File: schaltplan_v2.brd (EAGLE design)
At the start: 101 x 80 mm, 42 parts, among them T1 2N3565, T2 2N3565, T3 2N3565, T4 2N3565, T5 2N3565, T6 2N3565, T7 2N3565, T8 2N3565

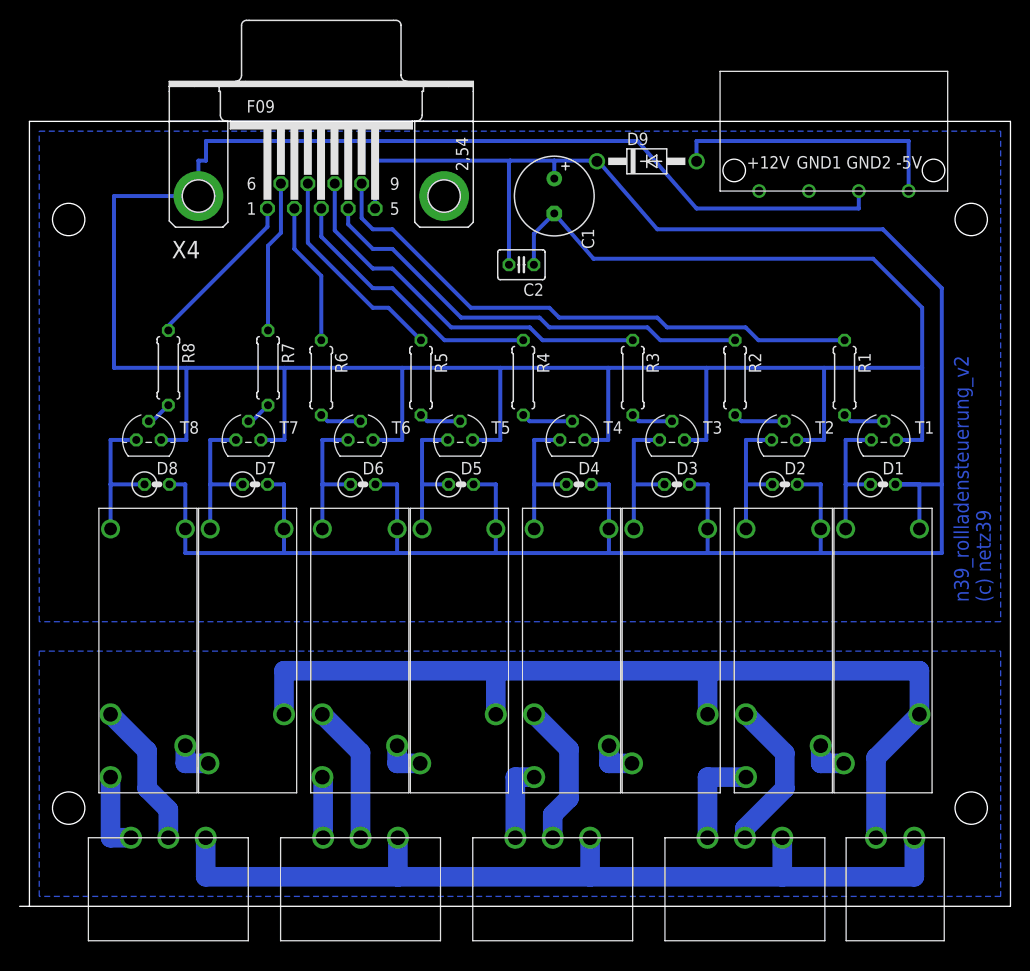
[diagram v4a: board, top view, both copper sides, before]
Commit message: fix ERC issues and schematic, reroute some signals
overall connection was lost due to some signal renamings, some parts
were not connected at all. additionally added restrict area around drill
holes
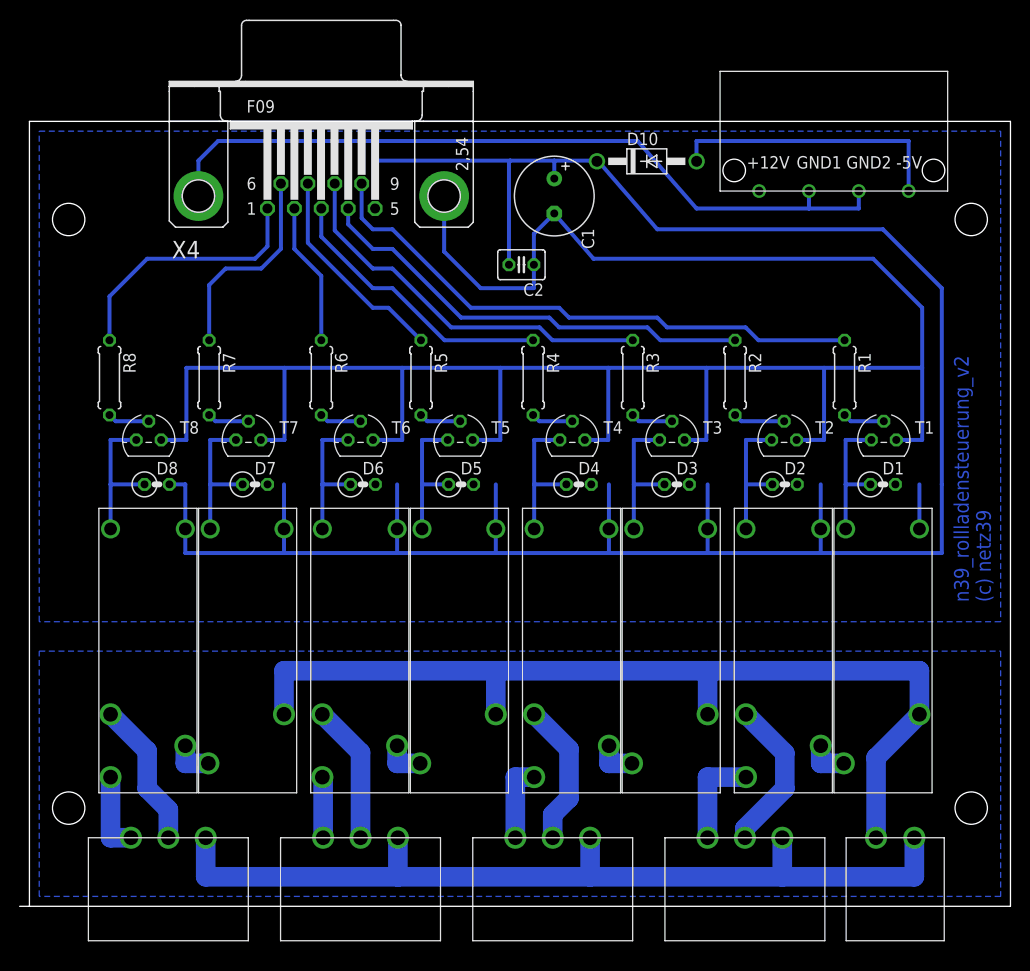
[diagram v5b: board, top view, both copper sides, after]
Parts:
- moved R7 6.08 mm to (18.3, 53.9)
- moved R8 6.08 mm to (8.16, 53.9)
- moved R4 1.00 mm to (51.3, 53.9)
- renumbered D9 to D10
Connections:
- removed net N$10: X4.G2
- net GND: now also U$14.GND1, X4.G2
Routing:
- net N$24: track 259.7 -> 235.4 mm
- net GND: track 319.8 -> 305.7 mm
- net N$15: track 16.6 -> 26.5 mm
- net N$21: track 15.5 -> 21.1 mm
- net N$48: track 2.68 -> 4.26 mm
- net N$40: track 2.68 -> 4.26 mm
- net N$28: track 5.26 -> 4.26 mm
- net N$23: track 27.8 -> 28.8 mm

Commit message: fix wrong connections in schematics
transitor pins were connected wrong and resistors are not diodes!
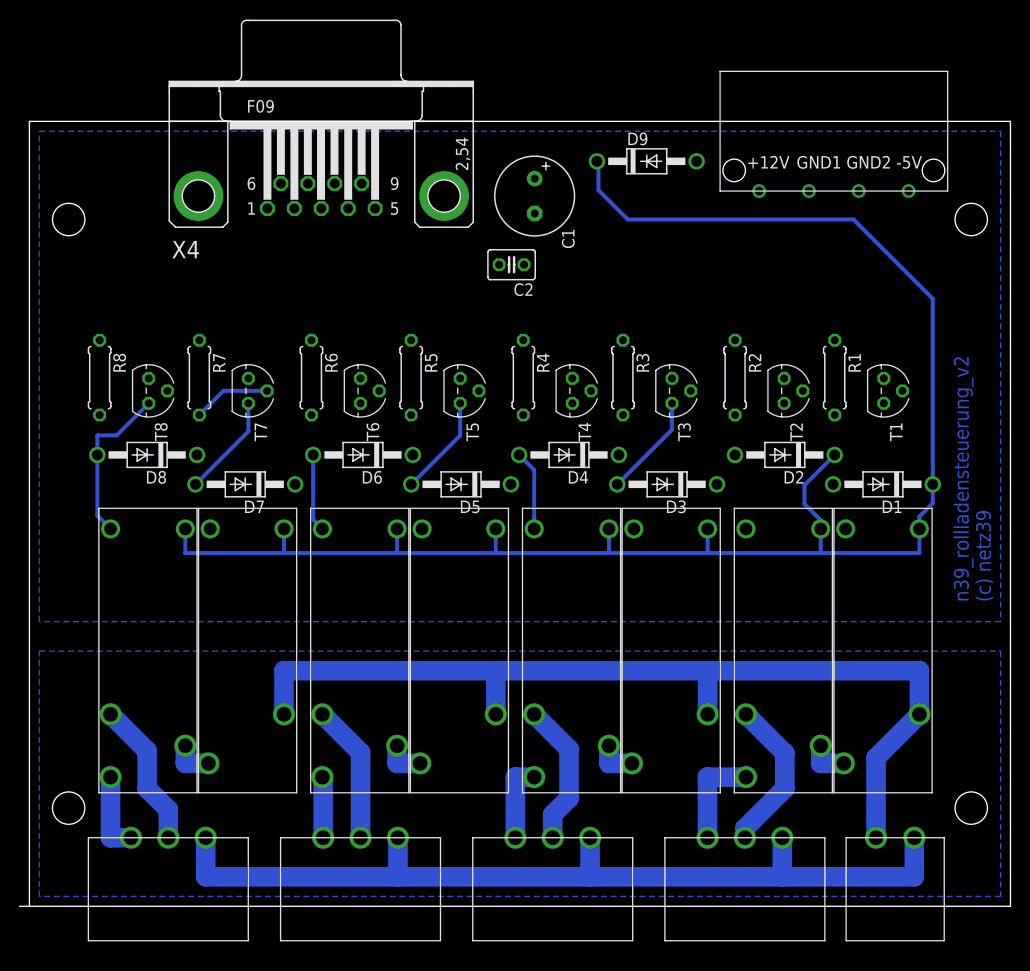
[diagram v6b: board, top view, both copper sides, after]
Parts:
- D1, D2, D3, D4, D5, D6, D7, D8: value (none) -> 1N4004; device rcl:0207/2V -> diode:DO41-10
- moved T1 5.00 mm to (87.1, 52.5), turned to 270 degrees
- moved T2 5.00 mm to (76.9, 52.5), turned to 270 degrees
- moved T3 5.00 mm to (65.5, 52.5), turned to 270 degrees
- moved T4 5.00 mm to (55.3, 52.5), turned to 270 degrees
- moved T5 5.00 mm to (43.9, 52.5), turned to 270 degrees
- moved T6 5.00 mm to (33.8, 52.5), turned to 270 degrees
- moved T7 5.00 mm to (22.3, 52.5), turned to 270 degrees
- moved T8 5.00 mm to (12.2, 52.5), turned to 270 degrees
- moved D4 3.16 mm to (55.0, 46.0), turned to 180 degrees
- moved D8 3.16 mm to (12.0, 46.0), turned to 180 degrees
- moved D2 3.00 mm to (77.0, 46.0), turned to 180 degrees
- moved D6 3.00 mm to (34.0, 46.0), turned to 180 degrees
- moved C1 2.00 mm to (51.5, 72.4)
- moved C2 1.00 mm to (49.1, 65.4)
- moved D3 1.00 mm to (65.0, 43.0), turned to 180 degrees
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- renumbered D10 to D9
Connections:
- removed net N$20: D3.1, T3.3, U$3.P$1
- removed net N$25: D4.1, T4.3, U$4.P$1
- removed net N$39: D6.1, T6.3, U$6.P$1
- removed net N$46: D7.1, T7.3, U$7.P$1
- removed net N$51: D8.1, T8.3, U$8.P$1
- new net N$10: D2.A, T2.1, U$2.P$1
- new net N$19: D4.A, T4.1, U$4.P$1
- new net N$33: D6.A, T6.1, U$6.P$1
- new net N$35: D8.A, T8.1, U$8.P$1
- new net V+: C1.+, C2.2, D1.C, D2.C, D3.C, D4.C, D5.C, D6.C, D7.C, D8.C, D9.C, U$1.P$2, U$2.P$2, U$3.P$2, U$4.P$2, U$5.P$2, U$6.P$2, U$7.P$2, U$8.P$2, X4.5
- net GND: now also T1.3, T2.3, T3.3, T4.3, T5.3, T6.3, T7.3, T8.3; no longer T1.1, T2.1, T3.1, T4.1, T5.1, T6.1, T7.1, T8.1
- net N$12: now also D3.A, T3.1, U$3.P$1; no longer D2.1, T2.3, U$2.P$1
- net N$24: now also D5.A, T5.1, U$5.P$1; no longer C1.+, C2.2, D1.2, D2.2, D3.2, D4.2, D5.2, D6.2, D7.2, D8.2, D9.C, U$1.P$2, U$2.P$2, U$3.P$2, U$4.P$2, U$5.P$2, U$6.P$2, U$7.P$2, U$8.P$2, X4.5
- net N$34: now also D7.A, T7.1, U$7.P$1; no longer D5.1, T5.3, U$5.P$1
- net N$6: now also D1.A, T1.1; no longer D1.1, T1.3
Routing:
- net GND: track 305.7 -> 0.00 mm
- net N$24: track 235.4 -> 10.3 mm
- net V+: track 0.00 -> 169.8 mm
- net N$38: track 57.9 -> 0.00 mm
- net N$26: track 45.9 -> 0.00 mm
- net N$37: track 39.8 -> 0.00 mm
- net N$23: track 28.8 -> 0.00 mm
- net N$7: track 28.8 -> 0.00 mm
- net N$15: track 26.5 -> 0.00 mm
- net N$11: track 21.7 -> 0.00 mm
- net N$21: track 21.1 -> 0.00 mm
- net N$35: track 0.00 -> 16.6 mm
- net N$51: track 15.2 -> 0.00 mm
- net N$46: track 15.0 -> 0.00 mm
- net N$25: track 15.0 -> 0.00 mm
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
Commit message: routing
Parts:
- moved D9 18.4 mm to (78.9, 66.9)
- moved C1 9.22 mm to (58.5, 66.4), turned to 90 degrees
- moved U$14 5.10 mm to (77.0, 80.0)
- moved C2 2.24 mm to (51.1, 66.4), turned to 270 degrees
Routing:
- net N$38: track 0.00 -> 56.9 mm
- net V+: track 169.8 -> 226.5 mm
- net N$26: track 0.00 -> 45.9 mm
- net N$37: track 0.00 -> 38.8 mm
- net N$23: track 0.00 -> 27.8 mm
- net N$15: track 0.00 -> 22.7 mm
- net N$11: track 0.00 -> 20.7 mm
- net N$21: track 0.00 -> 19.4 mm
- net N$6: track 0.00 -> 15.5 mm
- net N$10: track 0.00 -> 15.3 mm
- net N$14: track 0.00 -> 14.2 mm
- net N$8: track 0.00 -> 7.92 mm
- net N$36: track 0.00 -> 7.92 mm
- net N$22: track 0.00 -> 7.92 mm
- net N$13: track 0.00 -> 7.92 mm
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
